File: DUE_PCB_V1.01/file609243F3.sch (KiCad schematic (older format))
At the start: 24 parts, among them J29 Motor_Right1, J30 Motor_Right2, J31 Motor_Left1, J32 Motor_Left2, J33 Cutter_Motor, J34 ODORight1, J35 ODORight2, J36 ODOLeft1, J37 ODOLeft2, J38 ODOCutter

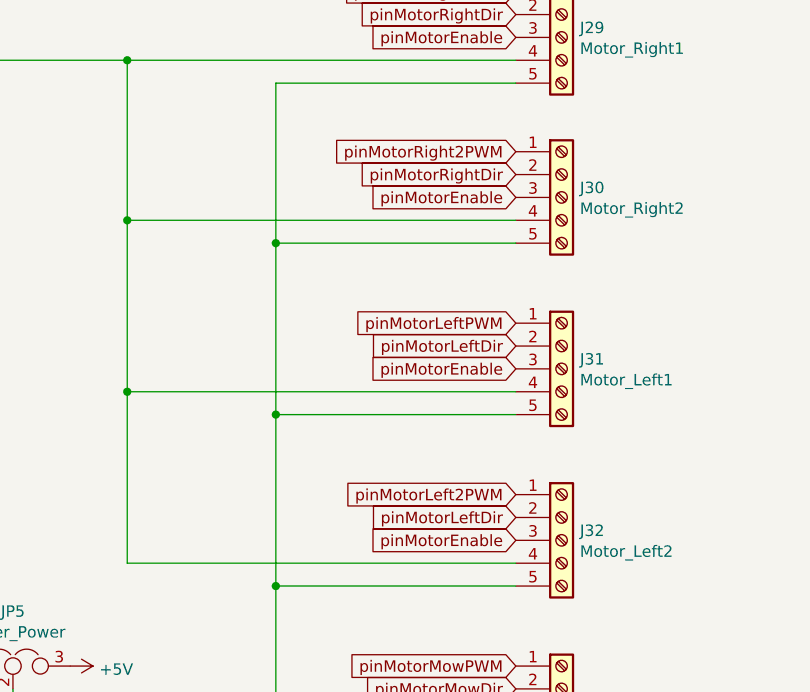
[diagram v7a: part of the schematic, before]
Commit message: Start ro add Bernard changes from 1.02
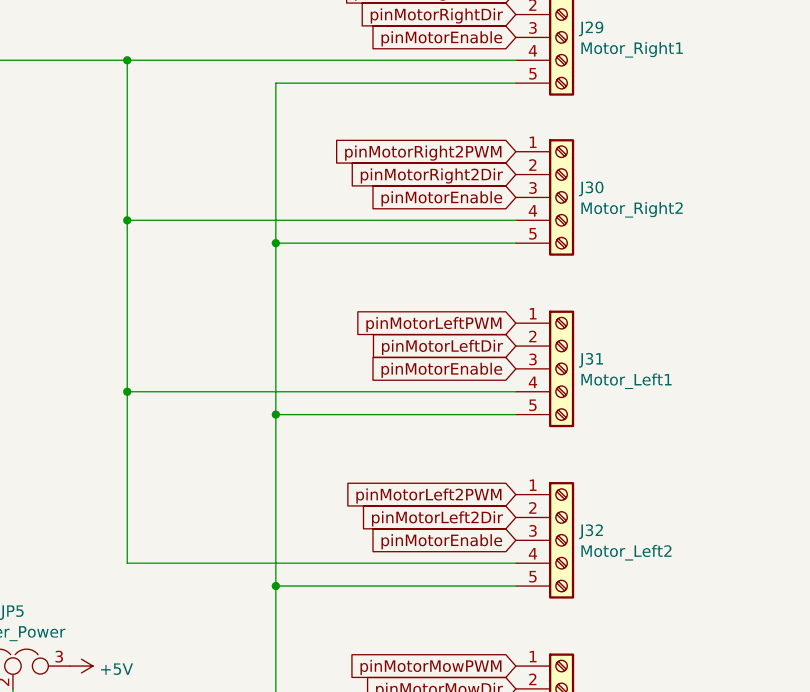
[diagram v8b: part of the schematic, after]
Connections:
- net pinMotorLeftDir: no longer J32.2 (Pin_2)
- net pinMotorRightDir: no longer J30.2 (Pin_2)
- new net pinMotorLeft2Dir: J32.2 (Pin_2)
- new net pinMotorRight2Dir: J30.2 (Pin_2)
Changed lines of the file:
@@
 pinMotorMowEnable
 Text GLabel 4150 1700 0    50   Input ~ 0
-pinMotorRightDir
+pinMotorRight2Dir
 Text GLabel 4150 3200 0    50   Input ~ 0
-pinMotorLeftDir
+pinMotorLeft2Dir
 $Comp
 L power:GND #PWR?
